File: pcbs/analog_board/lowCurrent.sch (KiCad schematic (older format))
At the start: 13 parts, among them P6 CONN_01X03, P7 CONN_01X03, U2 AD8616

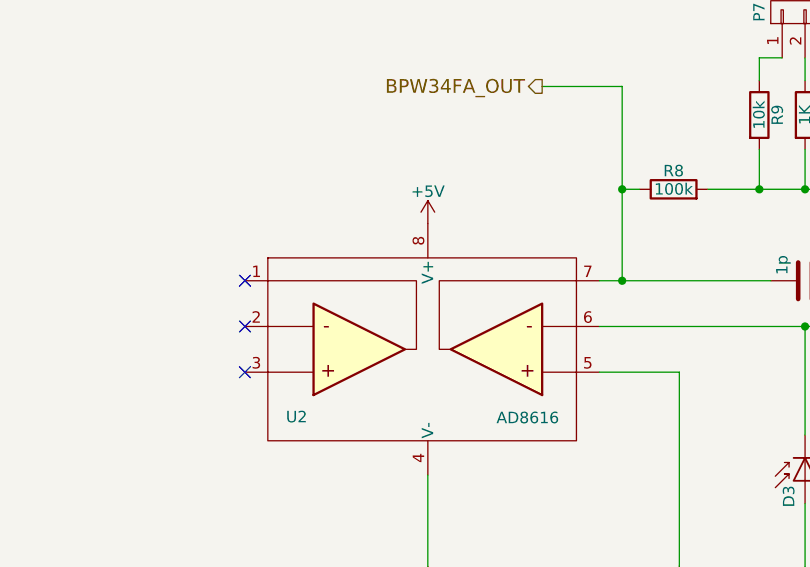
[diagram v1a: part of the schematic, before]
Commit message: Almost done with the etching machine CAD work.
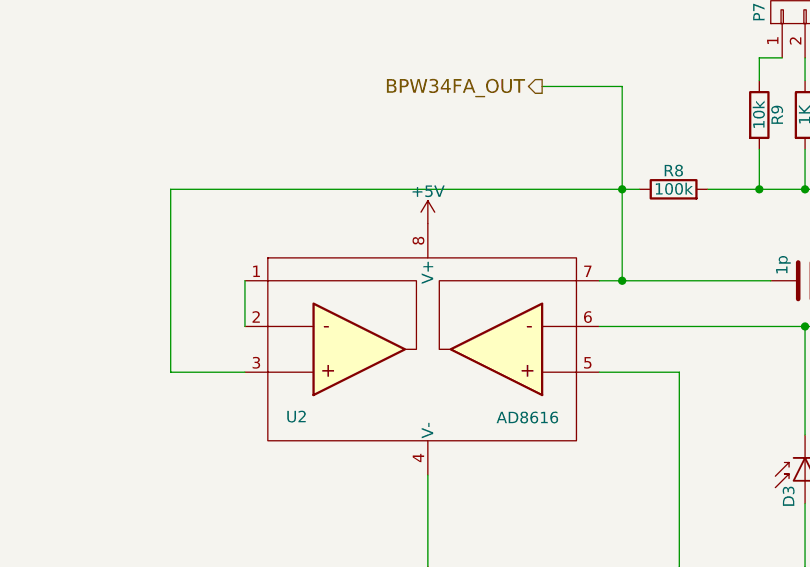
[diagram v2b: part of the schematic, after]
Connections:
- net BPW34FA_OUT: now also U2.3
- net at U2.1: now also U2.2
- no-connect marks 3 -> 0
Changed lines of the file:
@@
 	-1   0    0    -1
 $EndComp
-NoConn ~ 4425 4400
-NoConn ~ 4425 4200
-NoConn ~ 4425 4000
 $Comp
 L R R12
@@
 Connection ~ 6875 4200
 Wire Wire Line
-	6150 3600 6075 3600
+	4100 3600 6150 3600
 Wire Wire Line
 	5975 4000 6725 4000
@@
 	6075 3150 5725 3150
 Connection ~ 6075 3600
+Wire Wire Line
+	4425 4000 4425 4200
+Wire Wire Line
+	4100 3600 4100 4400
+Wire Wire Line
+	4100 4400 4425 4400
 $EndSCHEMATC
